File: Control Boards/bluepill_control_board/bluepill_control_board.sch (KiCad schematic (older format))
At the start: 2 parts, among them J1 Conn_01x26, U1 BluePill_STM32F103C

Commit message: Updated bluepill board for 30pin ribbon cable
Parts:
- removed J1: Conn_01x26, Connector_FFC-FPC:Hirose_FH12-26S-0.5SH_1x26-1MP_P0.50mm_Horizontal, symbol Connector_Generic:Conn_01x26
- added J1: Conn_01x30, Connector_FFC-FPC:Hirose_FH12-30S-0.5SH_1x30-1MP_P0.50mm_Horizontal, symbol Connector_Generic:Conn_01x30
- U1: symbol keyboard:BluePill_STM32F103C -> bluepill_control_board-rescue:BluePill_STM32F103C-keyboard
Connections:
- net +3V3: now also J1.1 (Pin_1), J1.24 (Pin_24)
- net +5V: now also J1.26 (Pin_26)
- net GND: now also J1.2 (Pin_2), J1.25 (Pin_25)
- net LED0: now also J1.23 (Pin_23)
- net LED1: now also J1.22 (Pin_22)
- net LED2: now also J1.21 (Pin_21)
- net MUX0: now also U1.33 (PB5), J1.4 (Pin_4); no longer U1.15 (PB10_SCL2)
- net MUX1: now also U1.32 (PB4), J1.3 (Pin_3); no longer U1.16 (PB11_SDA2)
- net MUX2: now also U1.36 (PB8), J1.5 (Pin_5); no longer U1.14 (PB1)
- net MUX3: now also U1.37 (PB9), J1.6 (Pin_6); no longer U1.13 (PB0)
- net RGB0: now also J1.12 (Pin_12)
- net RGB1: now also J1.13 (Pin_13)
- net RGB2: now also J1.14 (Pin_14)
- net RGB3: now also J1.15 (Pin_15)
- net RGB4: now also J1.16 (Pin_16)
- net ROW0: now also J1.11 (Pin_11)
- net ROW1: now also J1.10 (Pin_10)
- net ROW2: now also J1.9 (Pin_9)
- net ROW3: now also J1.8 (Pin_8)
- net ROW4: now also J1.7 (Pin_7)
- net SCL: now also J1.19 (Pin_19)
- net SDA: now also J1.20 (Pin_20)
- net USB_D+: now also J1.17 (Pin_17)
- net USB_D-: now also J1.18 (Pin_18)
- new net MOUSE_X: J1.27 (Pin_27), U1.13 (PB0)
- new net MOUSE_Y: J1.28 (Pin_28), U1.14 (PB1)
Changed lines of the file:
@@
 $EndDescr
 $Comp
-L keyboard:BluePill_STM32F103C U1
+L bluepill_control_board-rescue:BluePill_STM32F103C-keyboard U1
 U 1 1 61986373
 P 5200 3625
@@
 	1    5200 3625
 	1    0    0    -1
-$EndComp
-$Comp
-L Connector_Generic:Conn_01x26 J1
-U 1 1 6198690D
-P 8275 3950
-F 0 "J1" H 8355 3942 50  0000 L CNN
-F 1 "Conn_01x26" H 8355 3851 50  0000 L CNN
-F 2 "Connector_FFC-FPC:Hirose_FH12-26S-0.5SH_1x26-1MP_P0.50mm_Horizontal" H 8275 3950 50  0001 C CNN
-F 3 "~" H 8275 3950 50  0001 C CNN
-	1    8275 3950
-	1    0    0    1
 $EndComp
 $Comp
@@
 Text Label 4350 4025 2    50   ~ 0
 ROW4
-Text Label 4350 4125 2    50   ~ 0
+Text Label 6100 3225 0    50   ~ 0
 MUX3
-Text Label 4350 4225 2    50   ~ 0
+Text Label 6100 3325 0    50   ~ 0
 MUX2
-Text Label 4350 4325 2    50   ~ 0
+Text Label 6100 3625 0    50   ~ 0
 MUX0
-Text Label 4350 4425 2    50   ~ 0
+Text Label 6100 3725 0    50   ~ 0
 MUX1
 Text Label 8075 4950 2    50   ~ 0
@@
 Text Label 8075 4150 2    50   ~ 0
 ROW0
+$Comp
+L Connector_Generic:Conn_01x30 J1
+U 1 1 5EA05AAB
+P 8275 3750
+F 0 "J1" H 8193 2025 50  0000 C CNN
+F 1 "Conn_01x30" H 8193 2116 50  0000 C CNN
+F 2 "Connector_FFC-FPC:Hirose_FH12-30S-0.5SH_1x30-1MP_P0.50mm_Horizontal" H 8275 3750 50  0001 C CNN
+F 3 "~" H 8275 3750 50  0001 C CNN
+	1    8275 3750
+	1    0    0    1
+$EndComp
+Text Label 8075 2550 2    50   ~ 0
+MOUSE_X
+Text Label 8075 2450 2    50   ~ 0
+MOUSE_Y
+Text Label 4350 4225 2    50   ~ 0
+MOUSE_Y
+Text Label 4350 4125 2    50   ~ 0
+MOUSE_X
 $EndSCHEMATC

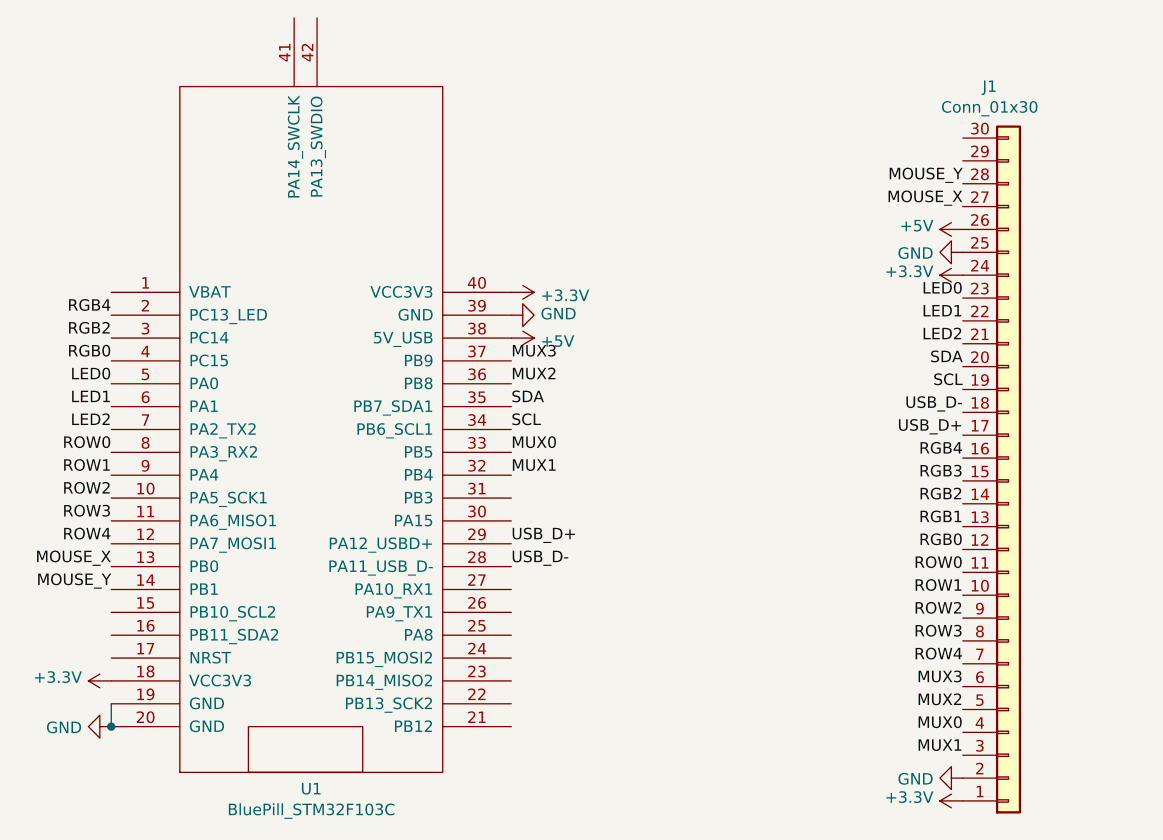
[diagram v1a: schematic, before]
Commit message: Added BOOT switch
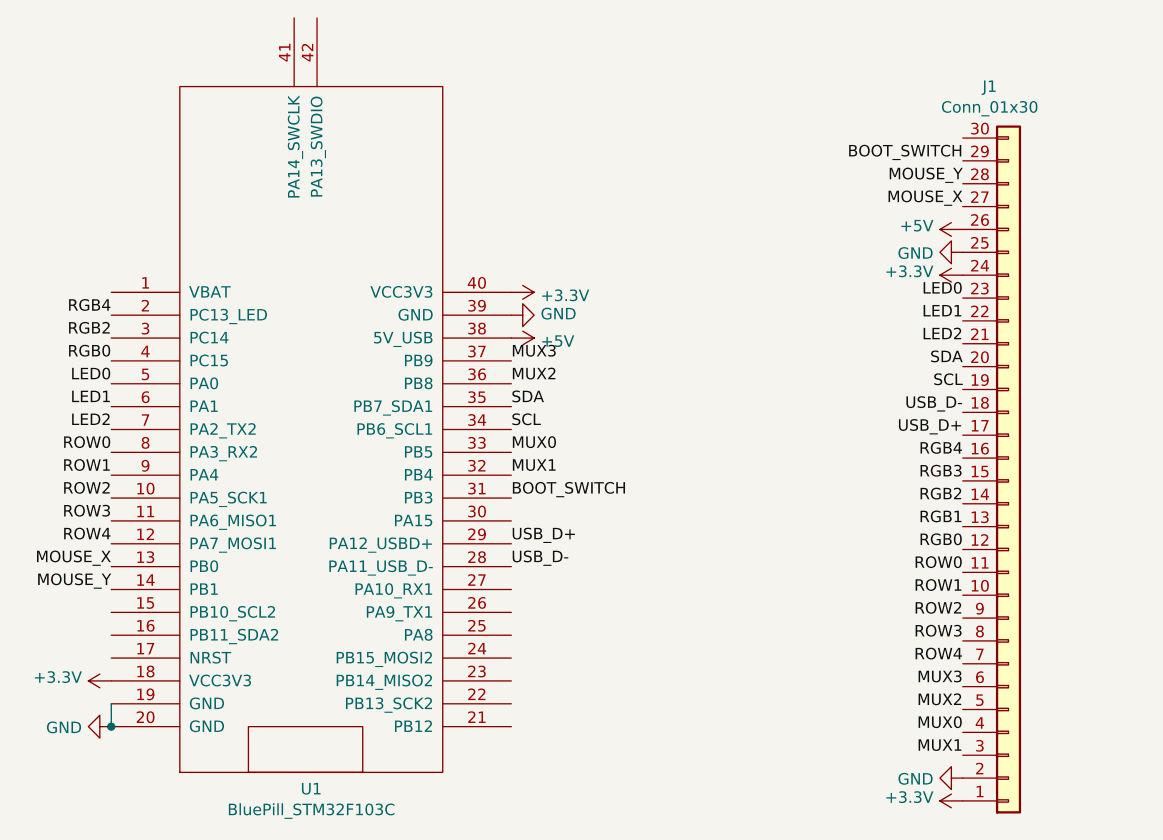
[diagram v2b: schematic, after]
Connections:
- net BOOT_SWITCH: now reaches J1.29 (Pin_29)
- net BOOT_SWITCH: now also U1.31 (PB3)
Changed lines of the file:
@@
 Text Label 4350 4125 2    50   ~ 0
 MOUSE_X
+Text Label 8075 2350 2    50   ~ 0
+BOOT_SWITCH
+Text Label 6100 3825 0    50   ~ 0
+BOOT_SWITCH
 $EndSCHEMATC
